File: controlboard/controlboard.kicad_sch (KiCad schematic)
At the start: 15 parts, among them J1 Conn_01x08, J1 ESP32-PICO-KIT, J2 LimitSwitch, J3 LimitSwitch, J4 LimitSwitch, J5 LimitSwitch, J6 Electromagnet, J7 Motor, J8 Motor, J9 Polulu Regulator 5V S13V20F5

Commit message: a
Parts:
- removed A1: Pololu_Breakout_DRV8825, Module:Pololu_Breakout-16_15.2x20.3mm, symbol Driver_Motor:Pololu_Breakout_DRV8825
- added C49: 100uF, symbol Device:C
- added R1: 4.7k, symbol Device:R
- A3: value Pololu_Breakout_DRV8825 -> Pololu_Breakout_DRV8834
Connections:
- net +12V: now also A3.8 (VMOT), J9.3 (Pin_3), C49.1
- net +5V: now also J9.1 (Pin_1)
- net GND: now also A3.1 (GND), A3.10 (M0), A3.11 (M1), A3.7 (GND), J9.2 (Pin_2), C49.2
- no-connect marks 0 -> 1
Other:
- note added: "ACTUATOR CONNECTIONS"
- note removed: "getting 3v from on-esp regulator"
- moved on the sheet: A3, C49, J1, J2, J3, J4, J5, J6, J7, J8, J9, U73

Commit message: updates to controlboard
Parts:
- removed A3: Pololu_Breakout_DRV8834, Module:Pololu_Breakout-16_15.2x20.3mm, symbol Driver_Motor:Pololu_Breakout_DRV8825
- removed C49: 100uF, symbol Device:C
- removed J1: ESP32-PICO-KIT, ESP32-PICO-KIT:XCVR_ESP32-PICO-KIT, symbol esp32-pico-kit:ESP32-PICO-KIT
- removed J2, J3, J4, J5: LimitSwitch, symbol Connector_Generic:Conn_01x03
- removed J9: Polulu Regulator 5V S13V20F5, symbol Connector_Generic:Conn_01x03
- removed JP33: Jumper_2_Open, symbol Jumper:Jumper_2_Open
- removed U73: ~, symbol chessbot-parts:Adafruit_HUSB238_Breakout
- added A1: Pololu_Breakout_MP6500, Module:Pololu_Breakout-16_15.2x20.3mm, symbol chessbot-parts:Pololu_Breakout_MP6500
- added A2: SilentStepStick TMC5160T, Module:Pololu_Breakout-16_15.2x20.3mm, symbol chessbot-parts:SilentStepStick
- added C10: C_Polarized, symbol Device:C_Polarized
- added D1: 1N4001, Diode_THT:D_DO-41_SOD81_P10.16mm_Horizontal, symbol Diode:1N4001
- added D4: D_Zener, symbol Device:D_Zener
- added J1: Raspberry_Pi_2_3, symbol Connector:Raspberry_Pi_2_3
- added J2, J3, J4, J5: LimitSwitch, symbol Connector_Generic:Conn_01x02
- added JP1: SolderJumper_2_Bridged, symbol Jumper:SolderJumper_2_Bridged
- added JP2, JP3: Jumper_3_Bridged12, symbol Jumper:Jumper_3_Bridged12
- added Q1: TODO, Package_TO_SOT_THT:TO-92_Inline, symbol Transistor_FET:2N7000
- added R10, R11, R13, R15: 10k, symbol Device:R
- added U2: CH224K, 0my_project:ESSOP-10_CH224K, symbol 0chessbot-parts:CH224K
- J6: value Electromagnet -> Electromagnet/Servo
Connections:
- net +5V: now also JP2.1 (A); no longer J1.8 (Pin_8)
- net GND: now also J6.3 (Pin_3), A1.1 (GND), A1.7 (GND), A2.1 (GND), A2.7 (GND), C10.2, J1.14 (GND), J1.20 (GND), J1.25 (GND), J1.30 (GND), J1.34 (GND), J1.39 (GND), J1.6 (GND), J1.9 (GND)
- net at J1.5 (Pin_5): now also JP1.1 (A)
- net at J6.2 (Pin_2): now also JP3.2 (C)
- net at J7.1 (Pin_1): now also A2.3 (1B)
- net at J7.2 (Pin_2): now also A2.4 (1A)
- net at J7.3 (Pin_3): now also A2.5 (2A)
- net at J7.4 (Pin_4): now also A2.6 (2B)
- net at J8.1 (Pin_1): now also A1.3 (1B)
- net at J8.2 (Pin_2): now also A1.4 (1A)
- net at J8.3 (Pin_3): now also A1.5 (2A)
- net at J8.4 (Pin_4): now also A1.6 (2B)
- new net: J5.2 (Pin_2), R15.2
- new net: J2.2 (Pin_2), R11.2
- new net: JP2.2 (C), JP3.1 (A), Q1.3 (D)
- new net: JP3.3 (B), Q1.1 (S)
- new net: J4.2 (Pin_2), R10.2
- new net: J3.2 (Pin_2), R13.2
- new net 3V3: JP1.2 (B)
- new net 5V: J1.2 (5V), J1.4 (5V), J1.8 (Pin_8)
- new net SW_1: R10.1
- new net SW_2: R11.1
- new net SW_3: R13.1
- new net SW_4: R15.1
- new net VIO: J2.1 (Pin_1), J3.1 (Pin_1), J4.1 (Pin_1), J5.1 (Pin_1)
- new net VMOT: A1.8 (VMOT), A2.8 (VMOT), C10.1
- new net Vdrive: JP2.3 (B)
- no-connect marks 1 -> 2
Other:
- added sheet Power (Power.kicad_sch)
- added sheet USB Hub (USB.kicad_sch)
- note added: "LED_IN is ~5V, BE CAREFUL"
- note added: "TODO am I getting this from 3.3V reg or Pi"
- note added: "TODO: overvoltage for pi 5V"
- note added: "These should be wired identically, I want the option to use SPI drivers or Step/Dir ones."
- moved on the sheet: J7, J8

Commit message: Control Board major progress
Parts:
- removed A1: Pololu_Breakout_MP6500, Module:Pololu_Breakout-16_15.2x20.3mm, symbol chessbot-parts:Pololu_Breakout_MP6500
- removed A2: SilentStepStick TMC5160T, Module:Pololu_Breakout-16_15.2x20.3mm, symbol chessbot-parts:SilentStepStick
- removed C10: C_Polarized, symbol Device:C_Polarized
- removed C49: 100uF, symbol Device:C
- removed D1: 1N4001, Diode_THT:D_DO-41_SOD81_P10.16mm_Horizontal, symbol Diode:1N4001
- removed J1: Conn_01x08, symbol Connector_Generic:Conn_01x08
- removed J1: Raspberry_Pi_2_3, symbol Connector:Raspberry_Pi_2_3
- removed J2, J3, J4, J5: LimitSwitch, symbol Connector_Generic:Conn_01x02
- removed J6: Electromagnet/Servo, symbol Connector_Generic:Conn_01x03
- removed J7, J8: Motor, symbol Connector_Generic:Conn_01x04
- removed JP1: SolderJumper_2_Bridged, symbol Jumper:SolderJumper_2_Bridged
- removed JP2, JP3: Jumper_3_Bridged12, symbol Jumper:Jumper_3_Bridged12
- removed Q1: TODO, Package_TO_SOT_THT:TO-92_Inline, symbol Transistor_FET:2N7000
- removed R1: 4.7k, symbol Device:R
- removed R10, R11, R13, R15: 10k, symbol Device:R
- removed U2: CH224K, 0my_project:ESSOP-10_CH224K, symbol 0chessbot-parts:CH224K
- added C2: 100n, symbol Device:C_Small
- added J27: GPIO, Connector_PinSocket_2.54mm:PinSocket_2x20_P2.54mm_Vertical, symbol Connector_Generic:Conn_02x20_Odd_Even
- added JP10: ID_WP, symbol Jumper:SolderJumper_2_Open
- added JP13, JP14, JP15, JP16, JP17: Jumper_2_Bridged, symbol Jumper:Jumper_2_Bridged
- added R1, R13: 3.9k, symbol Device:R_Small
- added U7: CAT24C256, symbol Memory_EEPROM:CAT24C256
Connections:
- net +5V: now also J27.2 (Pin_2), J27.4 (Pin_4)
- net GND: now also C2.2, J27.14 (Pin_14), J27.20 (Pin_20), J27.25 (Pin_25), J27.30 (Pin_30), J27.34 (Pin_34), J27.39 (Pin_39), J27.6 (Pin_6), J27.9 (Pin_9), U7.4 (GND)
- new net: JP10.1 (A), U7.7 (WP)
- new net: J27.1 (Pin_1), J27.17 (Pin_17)
- new net +3V3: C2.1, JP10.2 (B), R1.1, R13.1, U7.8 (VCC)
- new net CH_SCL: J27.5 (Pin_5)
- new net CH_SDA: J27.3 (Pin_3)
- new net CNC/(CS/I1)1: JP13.2 (B)
- new net CNC/(CS/I1)2: JP14.2 (B)
- new net CNC/SCK/MS2: JP16.2 (B)
- new net CNC/SDI/MS1: JP17.2 (B)
- new net CNC/SDO/I2: JP15.2 (B)
- new net DIR1: J27.8 (Pin_8)
- new net DIR2: J27.29 (Pin_29)
- new net ENBL: J27.36 (Pin_36)
- new net GPIO10/SPI0.MOSI: J27.19 (Pin_19)
- new net GPIO11/SPI0.SCLK: J27.23 (Pin_23)
- new net GPIO12/PWM0: J27.32 (Pin_32)
- new net GPIO13/PWM1: J27.33 (Pin_33)
- new net GPIO15/RXD0: J27.10 (Pin_10)
- new net GPIO17: J27.11 (Pin_11)
- new net GPIO18/PCM.CLK: J27.12 (Pin_12), JP13.1 (A)
- new net GPIO19/PCM.FS: J27.35 (Pin_35), JP15.1 (A)
- new net GPIO20/PCM.DIN: J27.38 (Pin_38), JP17.1 (A)
- new net GPIO21/PCM.DOUT: J27.40 (Pin_40), JP16.1 (A)
- new net GPIO22: J27.15 (Pin_15)
- new net GPIO23: J27.16 (Pin_16)
- new net GPIO24: J27.18 (Pin_18)
- new net GPIO25: J27.22 (Pin_22)
- new net GPIO26: J27.37 (Pin_37), JP14.1 (A)
- new net GPIO27: J27.13 (Pin_13)
- new net GPIO4/GPCLK0: J27.7 (Pin_7)
- new net GPIO6: J27.31 (Pin_31)
- new net GPIO7/SPI0.CE1: J27.26 (Pin_26)
- new net GPIO8/SPI0.CE0: J27.24 (Pin_24)
- new net GPIO9/SPI0.MISO: J27.21 (Pin_21)
- new net ID_SCL: J27.28 (Pin_28), R13.2, U7.6 (SCL)
- new net ID_SDA: J27.27 (Pin_27), R1.2, U7.5 (SDA)
- no-connect marks 2 -> 5
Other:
- added sheet CNC (cnc.kicad_sch)
- added sheet ChessBoard (chessboard.kicad_sch)
- added sheet How popular display hats connect (display_notes.kicad_sch)
- added sheet UI (ui.kicad_sch)
- note added: "ID_SD and ID_SC PINS: These pins are reserved for HAT ID EEPROM. At boot time this I2C interface will be interrogated to look for an EEPROM that identifes the attached board and allows automagic setup of the GPIOs (and optionally, Linux drivers). Bridging JP1 enables write protection. DO NOT USE these pins for anything other than attaching an I2C ID EEPROM. Leave unconnected if ID EEPROM not requ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"
- note added: "TODO: overvoltage fuse for pi 5V and 3.3V"
- note added: "current protection"
- note removed: "ACTUATOR CONNECTIONS"
- note removed: "LED_IN is ~5V, BE CAREFUL"
- note removed: "TODO: overvoltage for pi 5V"
- note removed: "These should be wired identically, I want the option to use SPI drivers or Step/Dir ones."
- moved on the sheet: D4

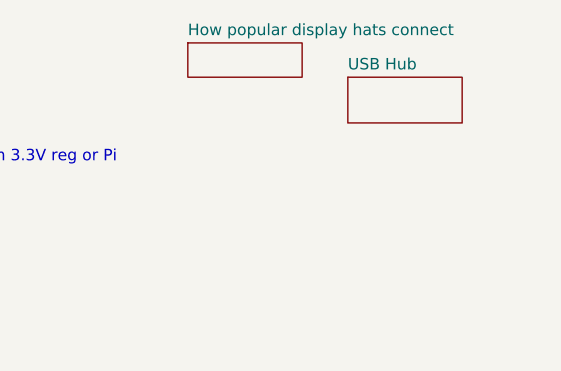
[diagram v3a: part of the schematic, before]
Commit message: remove USB
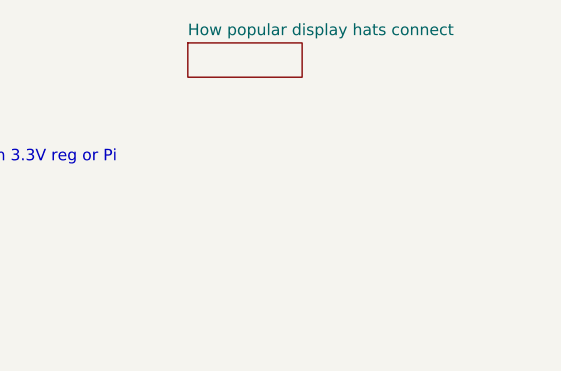
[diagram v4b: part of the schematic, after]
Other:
- removed sheet USB Hub
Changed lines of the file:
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@@
-	)
-	(sheet
-		(at 267.97 19.05)
-		(size 12.7 5.08)
-		(fields_autoplaced yes)
-		(stroke
-			(width 0.1524)
-			(type solid)
-		)
-		(fill
-			(color 0 0 0 0.0000)
-		)
-		(property "Sheetname" "USB Hub"
-			(at 267.97 18.3384 0)
-			(effects
-				(font
-					(size 1.27 1.27)
-				)
-				(justify left bottom)
-			)
-		)
-		(property "Sheetfile" "USB.kicad_sch"
-			(at 267.97 24.7146 0)
-			(effects
-				(font
-					(size 1.27 1.27)
-				)
-				(justify left top)
-				(hide yes)
-			)
-		)
-		(instances
-			(project "controlboard"
-				(path "/2797250d-6fee-4769-b4dd-0e20ce4f0941"
-					(page "3")
-				)
-			)
-		)
 	)
 	(sheet

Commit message: more progress on controlboard pcb
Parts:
- added D10, D11, D12, D13, D2, D3: LED, symbol Device:LED
- added R14, R15, R16, R17, R18, R2: 1k, symbol Device:R
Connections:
- net +5V: now also D3.2 (A)
- net GND: now also R14.1, R15.1, R16.1, R17.1, R18.1, R2.1
- net VDD: now also D10.2 (A)
- net Vdrive: now also D2.2 (A)
- new net: D11.1 (K), R16.2
- new net: D2.1 (K), R2.2
- new net: D13.1 (K), R18.2
- new net: D3.1 (K), R14.2
- new net: D10.1 (K), R15.2
- new net: D12.1 (K), R17.2
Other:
- note added: ".06A"
- note added: ".2A"
- note added: ".5A"
- note added: "12V: Max: 2A Nom: 1.4A"
- note added: "Lots of Status LEDs"
- note added: "Nom: .9A Max: 2.5A"
- note added: "Nominal case total current: 12V: 1.4A 5V: 2.3A 3V: .56A Summing: 3V: .6A (rounding up) 5V: 2.9A (+ .6A, LDO) 12V: 2.75A (+16W, Buck conv 90% efficient)"
- note added: "Pi: 1A - https://www.cnx-software.com/2021/12/09/raspberry-pi-zero-2-w-power-consumption/ USB: Max: 1A - (why? cuz i said so) Nom: .2A"
- note added: "TPS259631DDAR"
- note added: "WORST case total current: 12V: 2A 5V: 4.7A 3V: .56A Summing: 3V: .7A (rounding up) 5V: 5.4A (+ .7A, LDO) 12V: 4.5A (+30W, Buck conv 90% efficient) For reference, my laptop charger only does 12V 3A (or 20V 3A)"
- note added: "~0?"
- note removed: "TODO am I getting this from 3.3V reg or Pi"

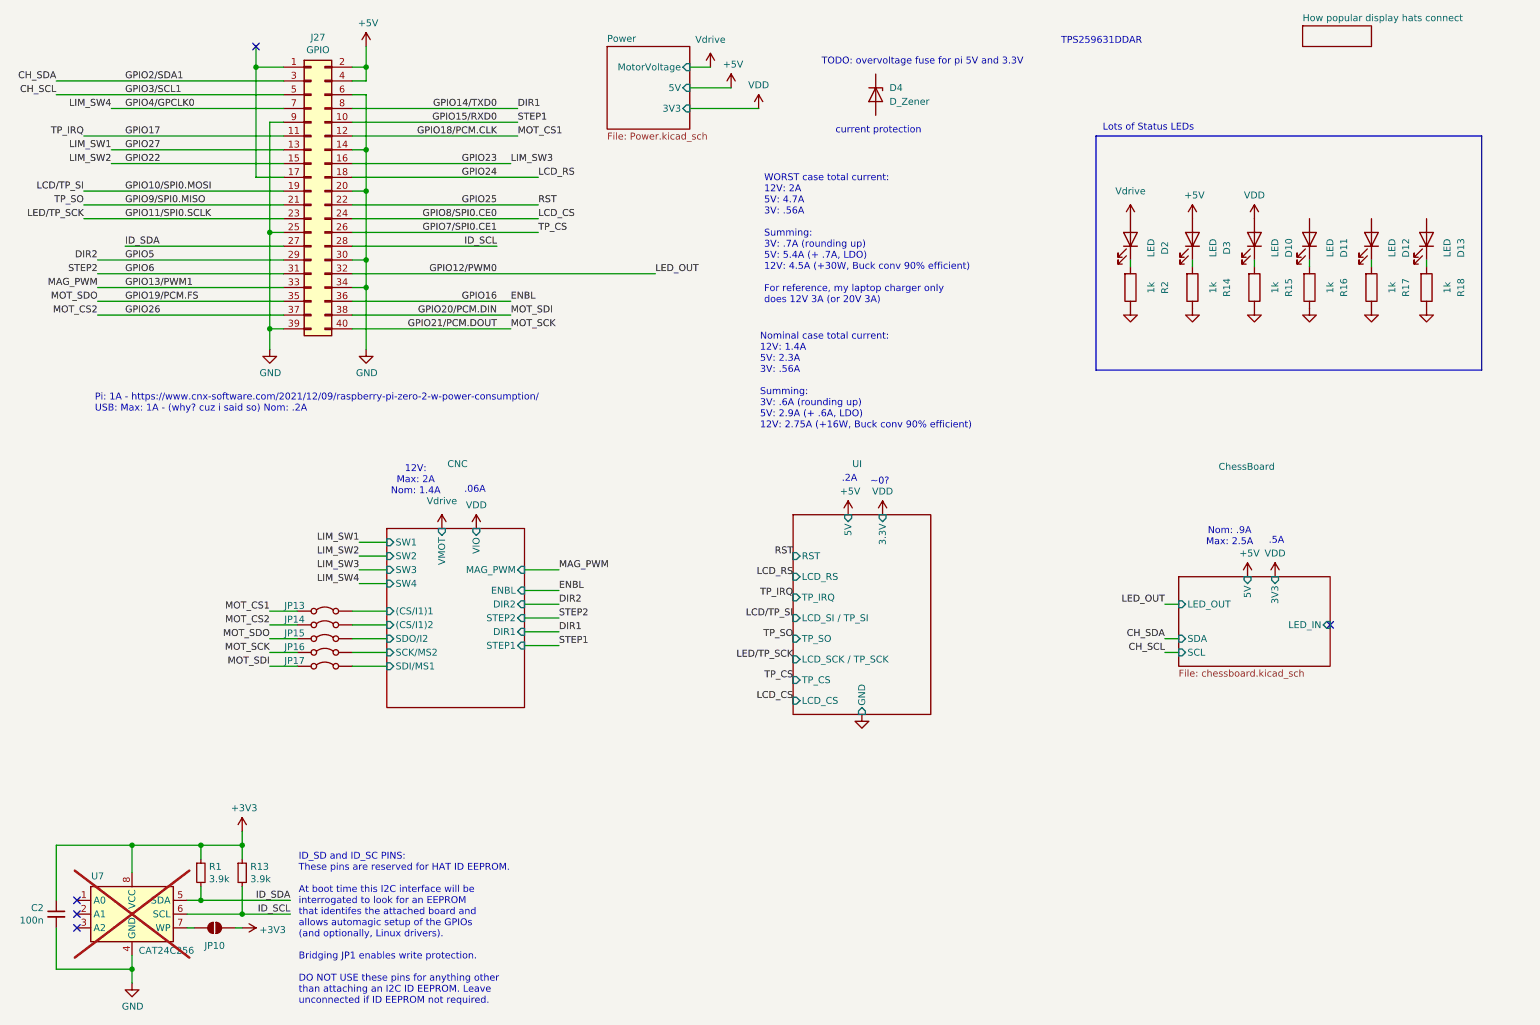
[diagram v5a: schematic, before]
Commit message: ControlBoard Schematic nearly done
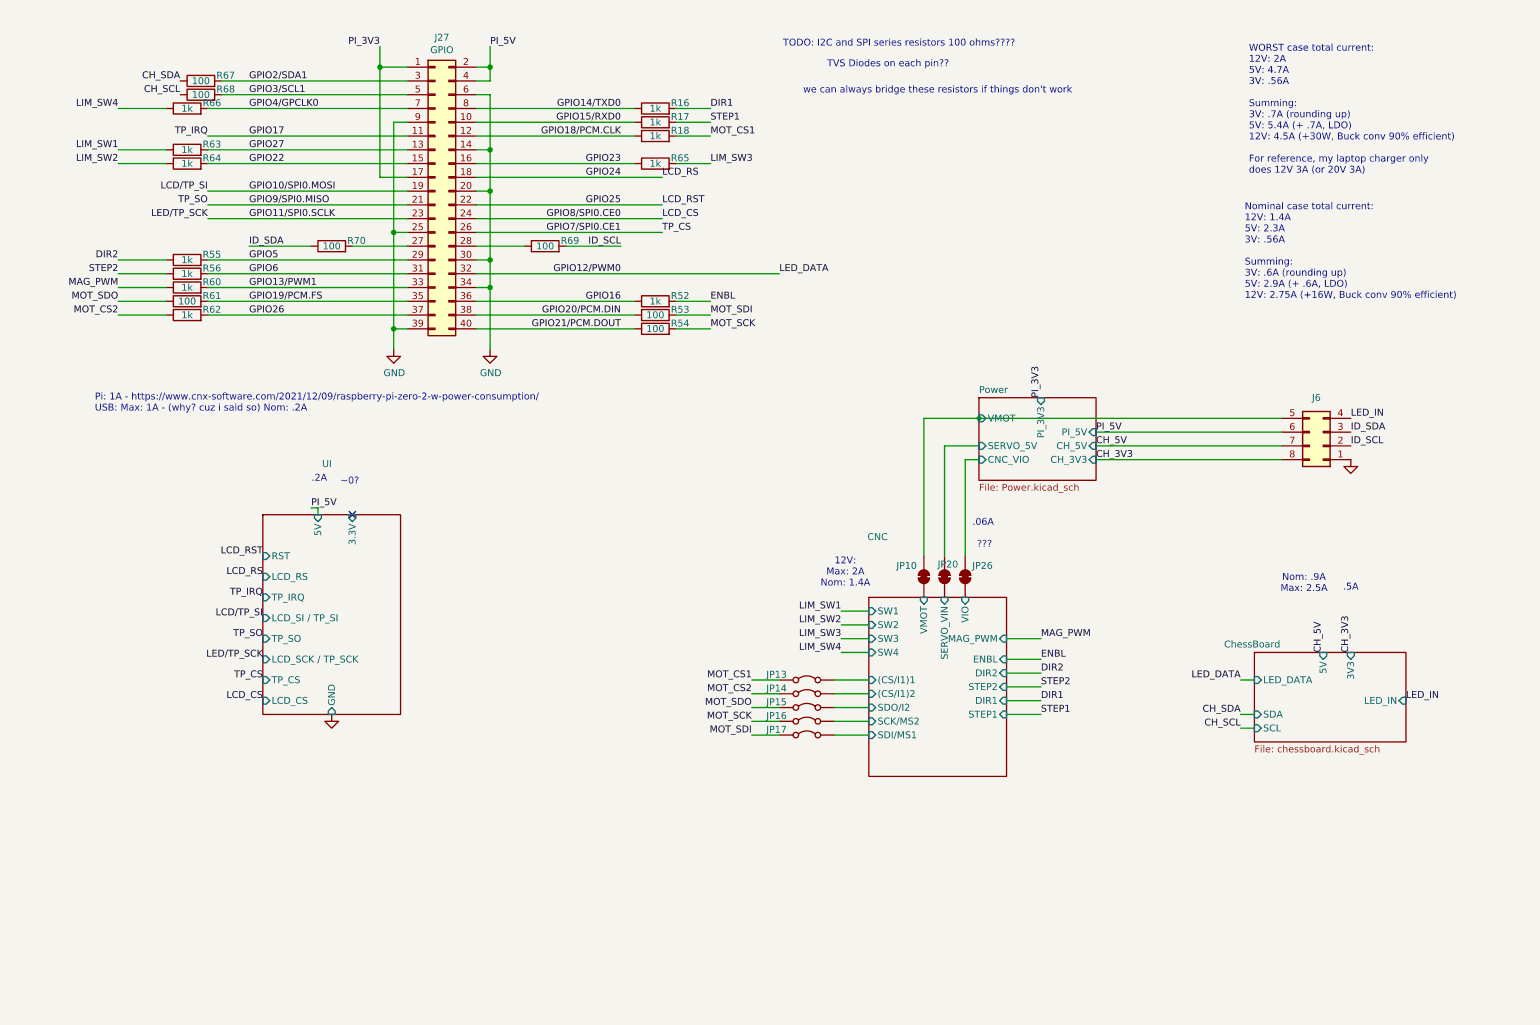
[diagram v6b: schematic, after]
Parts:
- removed C2: 100n, symbol Device:C_Small
- removed D10, D11, D12, D13, D2, D3: LED, symbol Device:LED
- removed D4: D_Zener, symbol Device:D_Zener
- removed JP10: ID_WP, symbol Jumper:SolderJumper_2_Open
- removed R1, R13: 3.9k, symbol Device:R_Small
- removed R14, R15, R2: 1k, symbol Device:R
- removed U7: CAT24C256, symbol Memory_EEPROM:CAT24C256
- added J6: Conn_02x04_Counter_Clockwise, Connector_PinSocket_2.54mm:PinSocket_2x04_P2.54mm_Horizontal, symbol Connector_Generic:Conn_02x04_Counter_Clockwise
- added JP10, JP20, JP26: SolderJumper_2_Bridged, Jumper:SolderJumper-2_P1.3mm_Bridged2Bar_RoundedPad1.0x1.5mm, symbol Jumper:SolderJumper_2_Bridged
- added R52, R55, R56, R60, R62, R63, R64, R65, R66: 1k, Resistor_SMD:R_0603_1608Metric_Pad0.98x0.95mm_HandSolder, symbol Device:R
- added R53, R54, R61, R67, R68, R69, R70: 100, Resistor_SMD:R_0603_1608Metric_Pad0.98x0.95mm_HandSolder, symbol Device:R
- J27: footprint Connector_PinSocket_2.54mm:PinSocket_2x20_P2.54mm_Vertical -> Connector_PinSocket_2.54mm:PinSocket_2x20_P2.54mm_Vertical_SMD
- JP13, JP14, JP15, JP16, JP17: footprint (none) -> TestPoint:TestPoint_2Pads_Pitch2.54mm_Drill0.8mm
- R16, R17, R18: footprint (none) -> Resistor_SMD:R_0603_1608Metric_Pad0.98x0.95mm_HandSolder
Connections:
- net CH_SCL: now also R68.1; no longer J27.5 (Pin_5)
- net CH_SDA: now also R67.1; no longer J27.3 (Pin_3)
- net DIR1: now also R16.2; no longer J27.8 (Pin_8)
- net DIR2: now also R55.1; no longer J27.29 (Pin_29)
- net ENBL: now also R52.2; no longer J27.36 (Pin_36)
- net GND: now also J6.1 (Pin_1); no longer R16.1, R17.1, R18.1
- net GPIO13/PWM1: now also R60.2
- net GPIO15/RXD0: now also R17.1
- net GPIO18/PCM.CLK: now also R18.1; no longer JP13.1 (A)
- net GPIO19/PCM.FS: now also R61.2; no longer JP15.1 (A)
- net GPIO20/PCM.DIN: now also R53.1; no longer JP17.1 (A)
- net GPIO21/PCM.DOUT: now also R54.1; no longer JP16.1 (A)
- net GPIO22: now also R64.2
- net GPIO23: now also R65.1
- net GPIO26: now also R62.2; no longer JP14.1 (A)
- net GPIO27: now also R63.2
- net GPIO4/GPCLK0: now also R66.2
- net GPIO6: now also R56.2
- net ID_SCL: now also J6.2 (Pin_2), R69.2; no longer J27.28 (Pin_28)
- net ID_SDA: now also J6.3 (Pin_3), R70.1; no longer J27.27 (Pin_27)
- net MOT_CS1: now reaches R18.2
- net MOT_CS1: now also JP13.1 (A)
- net PI_3V3: now reaches J27.1 (Pin_1), J27.17 (Pin_17)
- net STEP1: now reaches R17.2
- net +5V renamed PI_5V
- net PI_5V: now also J6.6 (Pin_6)
- new net: J27.28 (Pin_28), R69.1
- new net: J27.27 (Pin_27), R70.2
- new net CH_3V3: J6.8 (Pin_8)
- new net CH_5V: J6.7 (Pin_7)
- new net CNC/SERVO_VIN: JP20.1 (A)
- new net CNC/VIO: JP26.1 (A)
- new net CNC/VMOT: JP10.1 (A)
- new net GPIO14/TXD0: J27.8 (Pin_8), R16.1
- new net GPIO16: J27.36 (Pin_36), R52.1
- new net GPIO2/SDA1: J27.3 (Pin_3), R67.2
- new net GPIO3/SCL1: J27.5 (Pin_5), R68.2
- new net GPIO5: J27.29 (Pin_29), R55.2
- new net LED_IN: J6.4 (Pin_4)
- new net LIM_SW1: R63.1
- new net LIM_SW2: R64.1
- new net LIM_SW3: R65.2
- new net LIM_SW4: R66.1
- new net MAG_PWM: R60.1
- new net MOT_CS2: JP14.1 (A), R62.1
- new net MOT_SCK: JP16.1 (A), R54.2
- new net MOT_SDI: JP17.1 (A), R53.2
- new net MOT_SDO: JP15.1 (A), R61.1
- new net Power/CNC_VIO: JP26.2 (B)
- new net Power/SERVO_5V: JP20.2 (B)
- new net Power/VMOT: J6.5 (Pin_5), JP10.2 (B)
- new net STEP2: R56.1
- no-connect marks 5 -> 1
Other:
- removed sheet How popular display hats connect
- sheet CNC ports: added SERVO_VIN; removed none
- sheet ChessBoard ports: added LED_DATA; removed LED_OUT
- sheet Power ports: added CH_3V3, CH_5V, CNC_VIO, PI_3V3, PI_5V, SERVO_5V, VMOT; removed 3V3, 5V, MotorVoltage
- note added: "???"
- note added: "TODO: I2C and SPI series resistors 100 ohms????"
- note added: "TVS Diodes on each pin??"
- note added: "we can always bridge these resistors if things don't work"
- note removed: "ID_SD and ID_SC PINS: These pins are reserved for HAT ID EEPROM. At boot time this I2C interface will be interrogated to look for an EEPROM that identifes the attached board and allows automagic setup of the GPIOs (and optionally, Linux drivers). Bridging JP1 enables write protection. DO NOT USE these pins for anything other than attaching an I2C ID EEPROM. Leave unconnected if ID EEPROM not requ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"
- note removed: "Lots of Status LEDs"
- note removed: "TODO: overvoltage fuse for pi 5V and 3.3V"
- note removed: "TPS259631DDAR"
- note removed: "current protection"
- moved on the sheet: J27, JP13, JP14, JP15, JP16, JP17

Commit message: schematic improvements
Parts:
- added J10: Conn_01x02_Pin, symbol Connector:Conn_01x02_Pin
- added SW2: SW_Push TODO FP CHECK, Button_Switch_SMD:SW_SPST_SKQG_WithStem, symbol Switch:SW_Push
- added TP15: TestPoint, symbol Connector:TestPoint
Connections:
- net GND: now also J10.1 (Pin_1), SW2.2
- net ID_SCL: now also J10.2 (Pin_2), SW2.1
- net LED_IN: no longer names the net of J6.4 (Pin_4)
- new net ChessBoard/LED_IN: TP15.1
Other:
- sheet ChessBoard ports: added none; removed 3V3
- note added: "Soft shutdown button"
- note added: "TODO: 1. I2C and SPI series resistors 100 ohms???? 2. Do we need TVS Diodes on each pin??"
- note removed: "TODO: I2C and SPI series resistors 100 ohms????"
- note removed: "TVS Diodes on each pin??"
